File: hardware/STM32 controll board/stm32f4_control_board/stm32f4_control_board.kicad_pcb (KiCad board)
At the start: 2 copper layers, 47 parts, among them J1 Conn_01x06_Female, J2 USB_B_Micro, J3 Conn_01x40_Female, Q1 9013, SW1 SW_Push, U1 STM32F407VGTx, U2 STMPS2141, Y1 8MHz

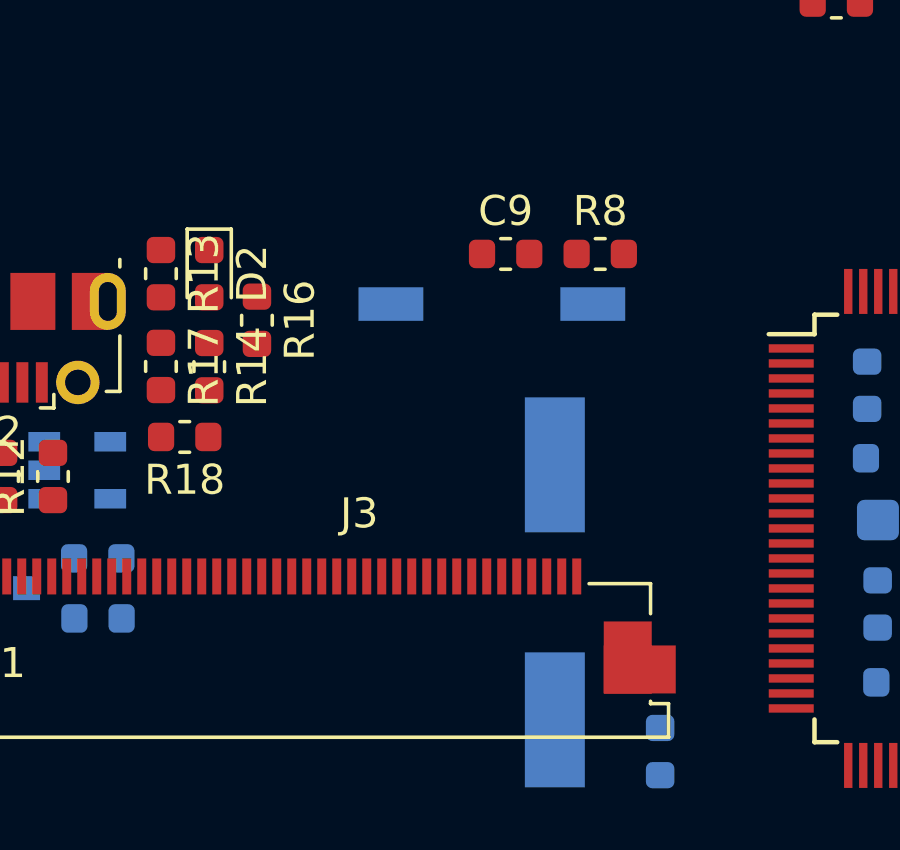
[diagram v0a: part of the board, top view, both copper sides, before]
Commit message: Ribbon connector and 3v LR
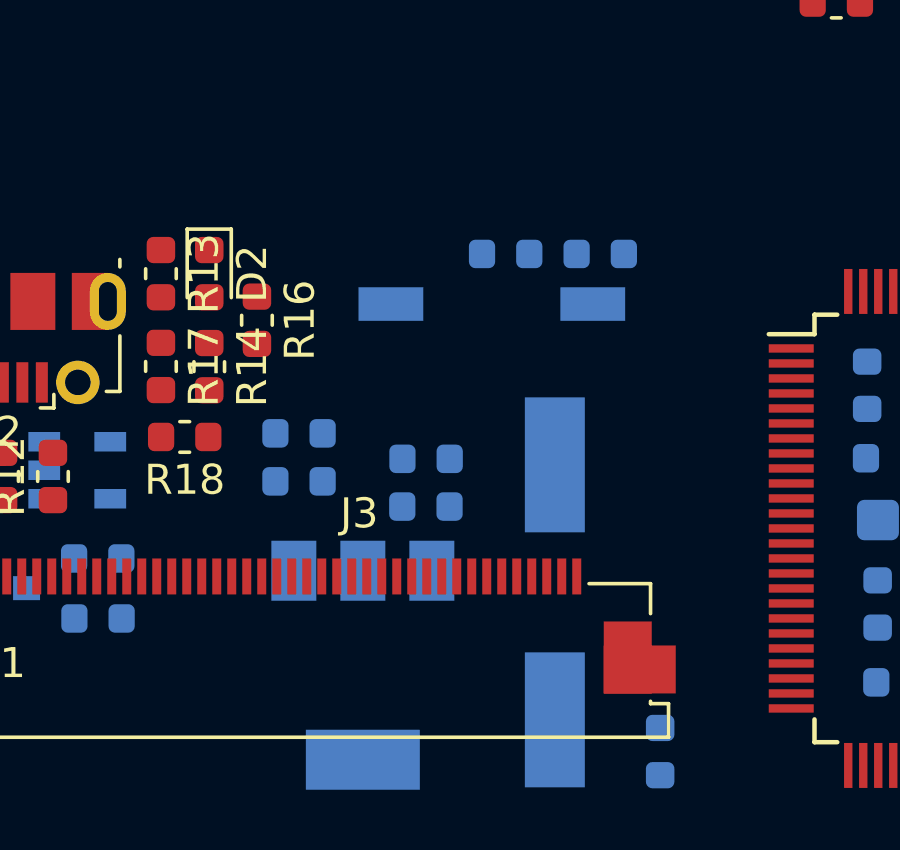
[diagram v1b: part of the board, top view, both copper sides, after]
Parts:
- added C19: 1uF, Capacitor_SMD:C_0603_1608Metric, B.Cu at (118.7, 126.7)
- added C20: 100nF, Capacitor_SMD:C_0603_1608Metric, B.Cu at (118.7, 128.3)
- added C21: 1uF, Capacitor_SMD:C_0603_1608Metric, B.Cu at (114.5, 125.9)
- added C22: 100nF, Capacitor_SMD:C_0603_1608Metric, B.Cu at (114.5, 127.5)
- added U3: AMS1117-3.3, Package_TO_SOT_SMD:SOT-223-3_TabPin2, B.Cu at (116.6, 133.6)
- C9, R8: moved to B.Cu
- J3: value Conn_01x40_Female -> Conn_01x26_Female
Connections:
- net PA10 renamed USB_OTG_ID
- net PA11 renamed USB_OTG_DM
- net PA12 renamed USB_OTG_DP
- net PA9 renamed USB_OTG_VBUS
- net PD5 renamed OTF_GS_overcurrent
- J3 pad 1: Net-(J3-Pad1) -> +5V
- J3 pad 10: Net-(J3-Pad10) -> GPIO9
- J3 pad 11: Net-(J3-Pad11) -> GPIO10
- J3 pad 12: Net-(J3-Pad12) -> GPIO11
- J3 pad 13: Net-(J3-Pad13) -> GPIO12
- J3 pad 14: Net-(J3-Pad14) -> UART2_TX
- J3 pad 15: Net-(J3-Pad15) -> UART2_RX
- J3 pad 16: Net-(J3-Pad16) -> UART2_CK
- J3 pad 17: Net-(J3-Pad17) -> I2C3_SDA
- J3 pad 18: Net-(J3-Pad18) -> I2C3_SCL
- J3 pad 19: Net-(J3-Pad19) -> SPI_MOSI
- J3 pad 2: Net-(J3-Pad2) -> USB_OTG_GND
- J3 pad 20: Net-(J3-Pad20) -> SPI_MISO
- J3 pad 21: Net-(J3-Pad21) -> SPI_SCK
- J3 pad 22: Net-(J3-Pad22) -> PB6-I2C1_SCL
- J3 pad 23: Net-(J3-Pad23) -> PB9-I2C1_SDA
- J3 pad 24: Net-(J3-Pad24) -> USB_OTG_GND
- J3 pad 25: Net-(J3-Pad25) -> +5V
- J3 pad 26: Net-(J3-Pad26) -> +3V3
- J3 pad 27: Net-(J3-Pad27) -> (no net)
- J3 pad 28: Net-(J3-Pad28) -> (no net)
- J3 pad 29: Net-(J3-Pad29) -> (no net)
- J3 pad 3: Net-(J3-Pad3) -> GPIO2
- J3 pad 30: Net-(J3-Pad30) -> (no net)
- J3 pad 31: Net-(J3-Pad31) -> (no net)
- J3 pad 32: Net-(J3-Pad32) -> (no net)
- J3 pad 33: Net-(J3-Pad33) -> (no net)
- J3 pad 34: Net-(J3-Pad34) -> (no net)
- J3 pad 35: Net-(J3-Pad35) -> (no net)
- J3 pad 36: Net-(J3-Pad36) -> (no net)
- J3 pad 37: Net-(J3-Pad37) -> (no net)
- J3 pad 38: Net-(J3-Pad38) -> (no net)
- J3 pad 39: Net-(J3-Pad39) -> (no net)
- J3 pad 4: Net-(J3-Pad4) -> GPIO3
- J3 pad 40: Net-(J3-Pad40) -> (no net)
- J3 pad 5: Net-(J3-Pad5) -> GPIO4
- J3 pad 6: Net-(J3-Pad6) -> GPIO5
- J3 pad 7: Net-(J3-Pad7) -> GPIO6
- J3 pad 8: Net-(J3-Pad8) -> GPIO7
- J3 pad 9: Net-(J3-Pad9) -> GPIO8
- U1 pad 1: Net-(U1-Pad1) -> GPIO5
- U1 pad 15: Net-(U1-Pad15) -> PC0
- U1 pad 16: Net-(U1-Pad16) -> GPIO2
- U1 pad 17: Net-(U1-Pad17) -> GPIO3
- U1 pad 18: Net-(U1-Pad18) -> GPIO4
- U1 pad 2: Net-(U1-Pad2) -> GPIO6
- U1 pad 23: Net-(U1-Pad23) -> GPIO10
- U1 pad 24: Net-(U1-Pad24) -> GPIO11
- U1 pad 25: Net-(U1-Pad25) -> UART2_TX
- U1 pad 26: Net-(U1-Pad26) -> UART2_RX
- U1 pad 29: Net-(U1-Pad29) -> GPIO12
- U1 pad 3: Net-(U1-Pad3) -> GPIO7
- U1 pad 30: Net-(U1-Pad30) -> SPI_SCK
- U1 pad 31: Net-(U1-Pad31) -> SPI_MISO
- U1 pad 32: Net-(U1-Pad32) -> SPI_MOSI
- U1 pad 4: Net-(U1-Pad4) -> GPIO8
- U1 pad 5: Net-(U1-Pad5) -> GPIO9
- U1 pad 66: Net-(U1-Pad66) -> I2C3_SDA
- U1 pad 67: Net-(U1-Pad67) -> I2C3_SCL
- U1 pad 88: Net-(U1-Pad88) -> UART2_CK
- U1 pad 92: PB6 -> PB6-I2C1_SCL
- U1 pad 96: PB9 -> PB9-I2C1_SDA
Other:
- rule trace_min: 0.2 -> 0.1
